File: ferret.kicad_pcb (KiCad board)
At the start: 4 copper layers, 50 x 50 mm, 135 parts, among them J201 Power, J301 BAT, J302 BAT, J304 SYS, J401 CTRL, J402 CHG, J403 SOICbite, J404 RS485, Q201 40V, Q202 40V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

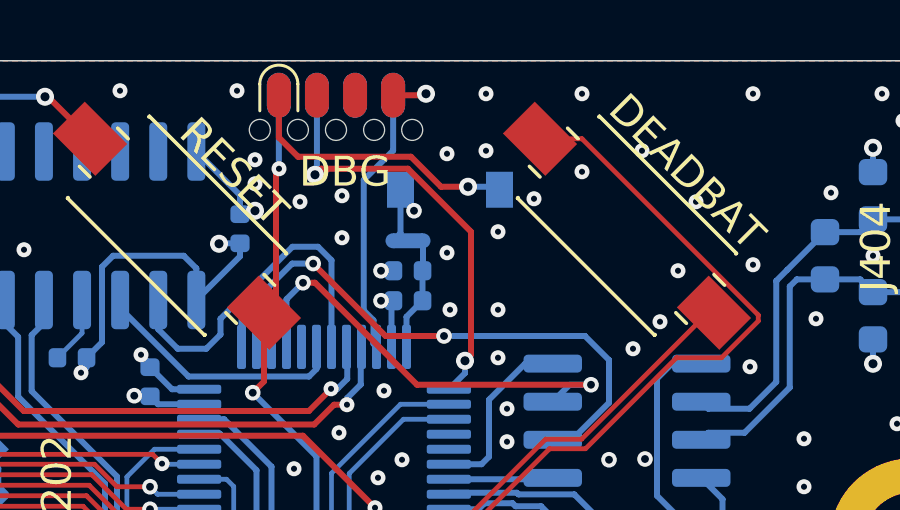
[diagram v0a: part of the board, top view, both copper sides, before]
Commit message: added missing JLC/LCSC parts
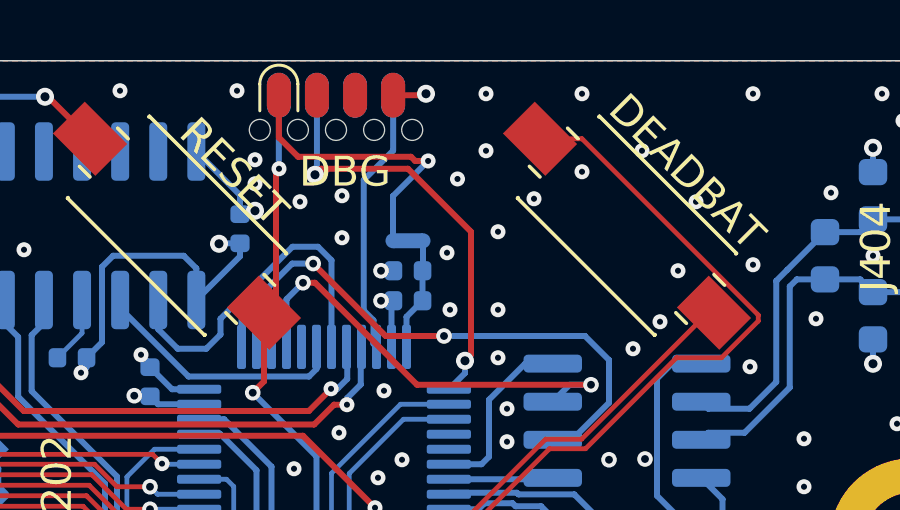
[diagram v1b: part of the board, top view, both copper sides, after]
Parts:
- removed D406: 5V, Diode_SMD:D_SOD-123
- R303: value 5.23k -> 5.1k
- R304: value 30.1k -> 30k
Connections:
- J401 pad A5: Net-(J401-PadA5) -> (no net)
- J401 pad A8: Net-(J401-PadA8) -> (no net)
- J401 pad B5: Net-(J401-PadB5) -> (no net)
- J401 pad B8: Net-(J401-PadB8) -> (no net)
- J403 pad 1: Net-(D406-Pad2) -> +3V3
- J403 pad 2: Net-(J403-Pad2) -> (no net)
- J403 pad 3: Net-(J403-Pad3) -> (no net)
- J403 pad 6: Net-(J403-Pad6) -> (no net)
- U202 pad 13: Net-(U202-Pad13) -> (no net)
- U202 pad 2: Net-(U202-Pad2) -> (no net)
- U202 pad 9: Net-(U202-Pad9) -> (no net)
- U401 pad 15: Net-(U401-Pad15) -> (no net)
- U401 pad 26: /Control/EXT_SCL -> (no net)
- U401 pad 27: /Control/EXT_SDA -> (no net)
- U401 pad 29: Net-(U401-Pad29) -> (no net)
- U401 pad 3: Net-(U401-Pad3) -> (no net)
- U401 pad 4: Net-(U401-Pad4) -> (no net)
- U401 pad 40: Net-(U401-Pad40) -> (no net)
- U401 pad 41: Net-(U401-Pad41) -> (no net)
- U402 pad 10: Net-(U402-Pad10) -> (no net)
- U402 pad 11: Net-(U402-Pad11) -> (no net)
- U402 pad 12: Net-(U402-Pad12) -> (no net)
- U402 pad 13: Net-(U402-Pad13) -> (no net)
- U402 pad 14: Net-(U402-Pad14) -> (no net)
- U402 pad 15: Net-(U402-Pad15) -> (no net)
- U402 pad 9: Net-(U402-Pad9) -> (no net)
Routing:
- net Net-(D406-Pad2): track 9.48 -> 0.00 mm, vias 1 -> 0
- net +3V3: track 97.8 -> 105.0 mm

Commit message: changed 127k to 120k
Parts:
- R301: value 127k -> 120k

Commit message: uups
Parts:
- U201: footprint Package_DFN_QFN:QFN-20-1EP_3x3mm_P0.4mm_EP1.65x1.65mm -> Automated:QFN-20-1EP_3x3mm_P0.4mm_EP1.65x1.65mm
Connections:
- J401 pad A5: (no net) -> Net-(J401-PadA5)
- J401 pad A8: (no net) -> Net-(J401-PadA8)
- J401 pad B5: (no net) -> Net-(J401-PadB5)
- J401 pad B8: (no net) -> Net-(J401-PadB8)
- J403 pad 2: (no net) -> Net-(J403-Pad2)
- J403 pad 3: (no net) -> Net-(J403-Pad3)
- J403 pad 6: (no net) -> Net-(J403-Pad6)
- U202 pad 13: (no net) -> Net-(U202-Pad13)
- U202 pad 2: (no net) -> Net-(U202-Pad2)
- U202 pad 9: (no net) -> Net-(U202-Pad9)
- U401 pad 15: (no net) -> Net-(U401-Pad15)
- U401 pad 26: (no net) -> /Control/EXT_SCL
- U401 pad 27: (no net) -> /Control/EXT_SDA
- U401 pad 29: (no net) -> Net-(U401-Pad29)
- U401 pad 3: (no net) -> Net-(U401-Pad3)
- U401 pad 4: (no net) -> Net-(U401-Pad4)
- U401 pad 40: (no net) -> Net-(U401-Pad40)
- U401 pad 41: (no net) -> Net-(U401-Pad41)
- U402 pad 10: (no net) -> Net-(U402-Pad10)
- U402 pad 11: (no net) -> Net-(U402-Pad11)
- U402 pad 12: (no net) -> Net-(U402-Pad12)
- U402 pad 13: (no net) -> Net-(U402-Pad13)
- U402 pad 14: (no net) -> Net-(U402-Pad14)
- U402 pad 15: (no net) -> Net-(U402-Pad15)
- U402 pad 9: (no net) -> Net-(U402-Pad9)

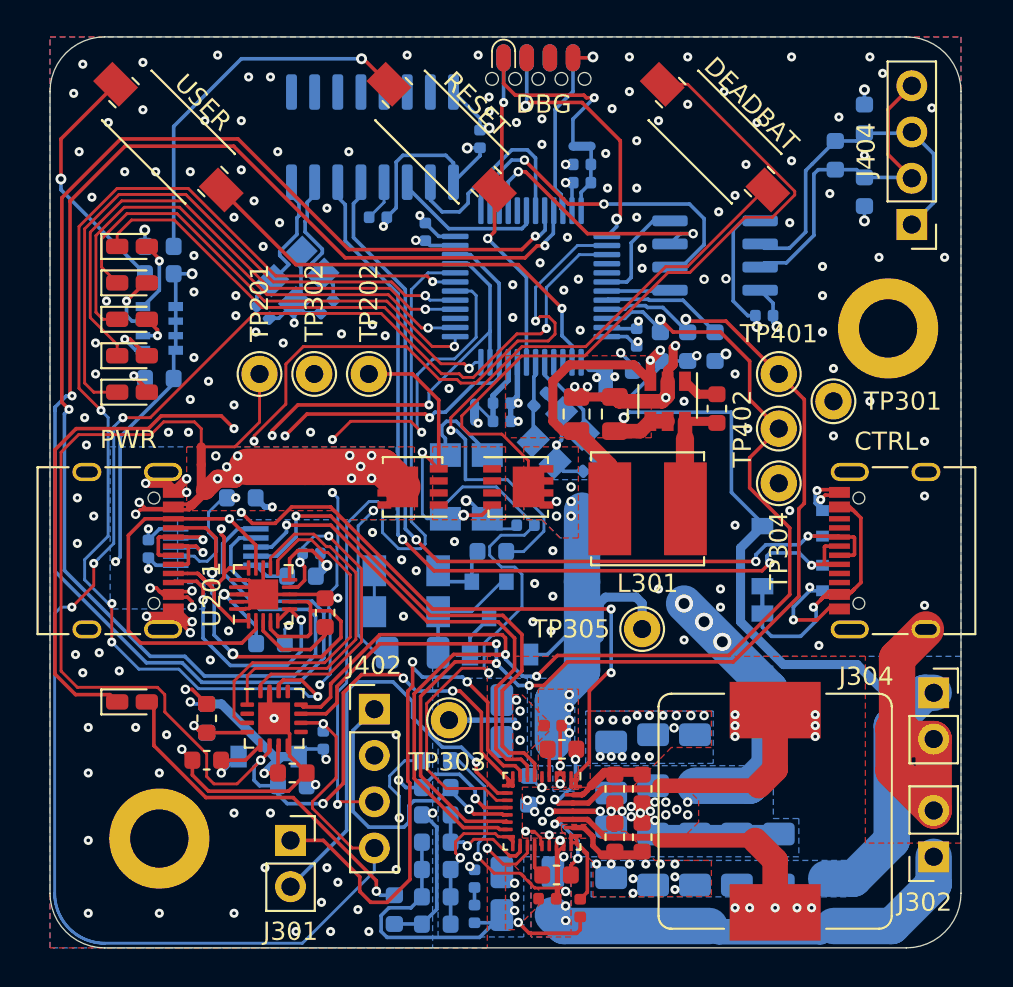
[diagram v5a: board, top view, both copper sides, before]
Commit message: added 3D models
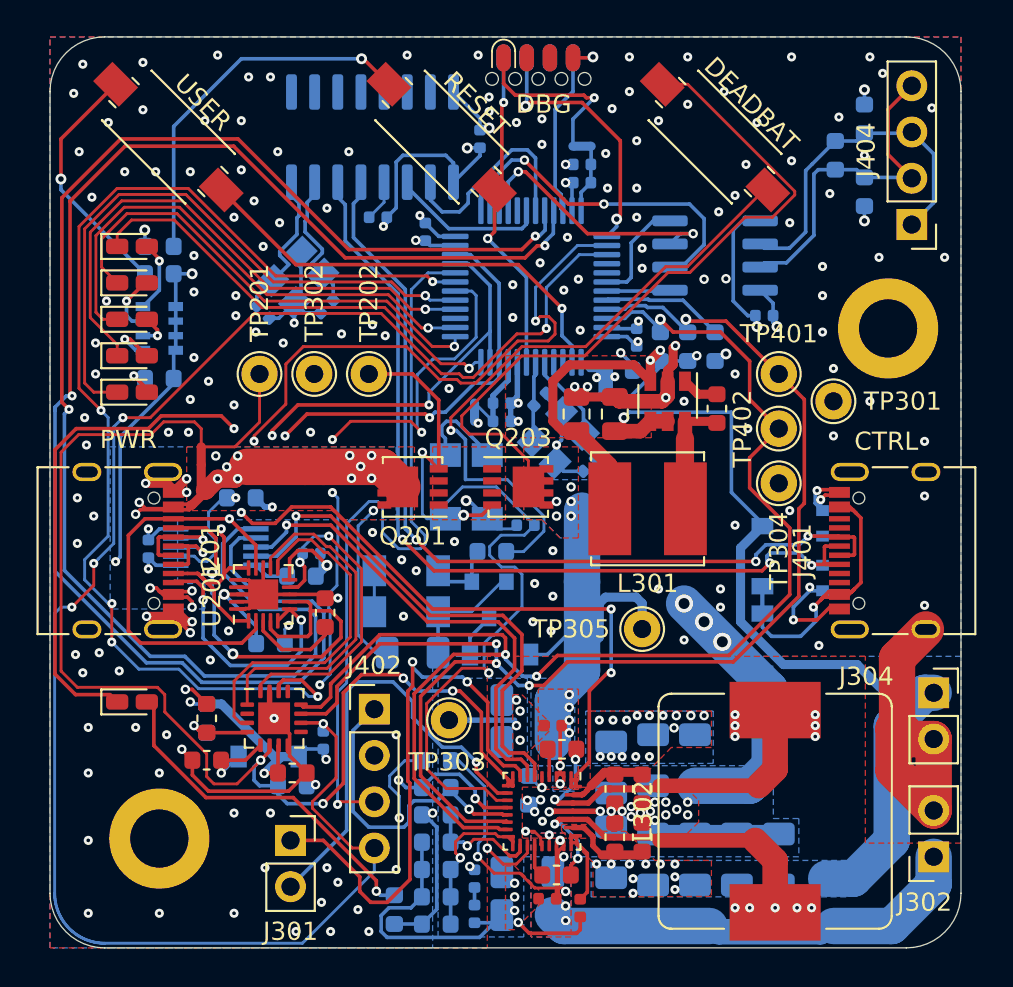
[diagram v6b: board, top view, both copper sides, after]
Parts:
- J201, J401: footprint Connector_USB:USB_C_Receptacle_XKB_U262-16XN-4BVC11 -> Automated:USB_C_Receptacle_XKB_U262-16XN-4BVC11
- L302: footprint Inductor_SMD:L_Bourns_SRP1245A -> Automated:L_Bourns_SRP1245A
- Q201, Q203: footprint Package_SO:Vishay_PowerPAK_1212-8_Single -> Automated:Vishay_PowerPAK_1212-8_Single
